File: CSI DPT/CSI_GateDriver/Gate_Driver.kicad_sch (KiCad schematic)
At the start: 75 parts, among them J1 SSW-102-01-G-D, J2 Conn_02x08_Odd_Even, J3 SSW-102-01-G-D, Q3 DMP3099L, U1 UCC23513QDWYRQ1, U10 UCC23513QDWYRQ1, U11 MGJ2D121802SC, U12 LDK130-12_SOT23_SOT353, U2 MGJ2D121802SC, U3 MGJ2D121802SC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

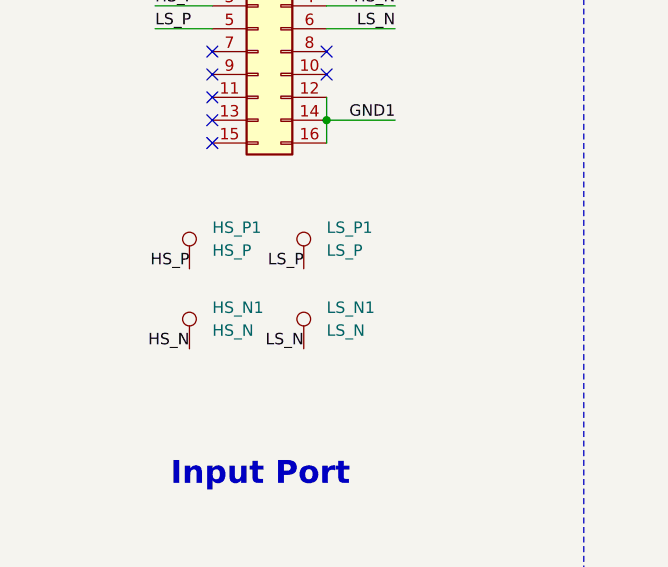
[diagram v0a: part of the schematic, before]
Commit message: Size down the boards
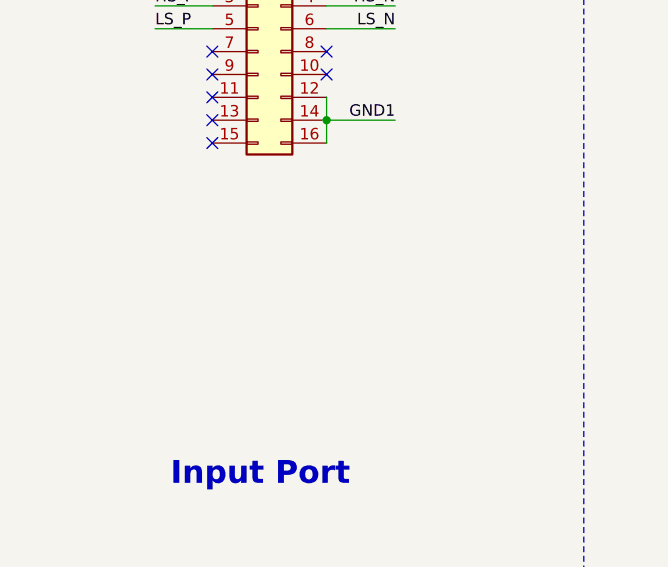
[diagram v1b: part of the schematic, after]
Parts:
- removed HS_N1: HS_N, TestPoint:TestPoint_Pad_D2.0mm, symbol Connector:TestPoint
- removed HS_P1: HS_P, TestPoint:TestPoint_Pad_D2.0mm, symbol Connector:TestPoint
- removed LS_N1: LS_N, TestPoint:TestPoint_Pad_D2.0mm, symbol Connector:TestPoint
- removed LS_P1: LS_P, TestPoint:TestPoint_Pad_D2.0mm, symbol Connector:TestPoint
